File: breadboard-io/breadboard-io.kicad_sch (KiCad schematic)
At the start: 29 parts, among them J1 Conn_01x10_Male, Q1 DMN3300U, Q2 DMN3300U, Q3 DMN3300U, Q4 DMN3300U, SW1 SW0, SW2 SW0, SW3 SW0, SW4 SW0

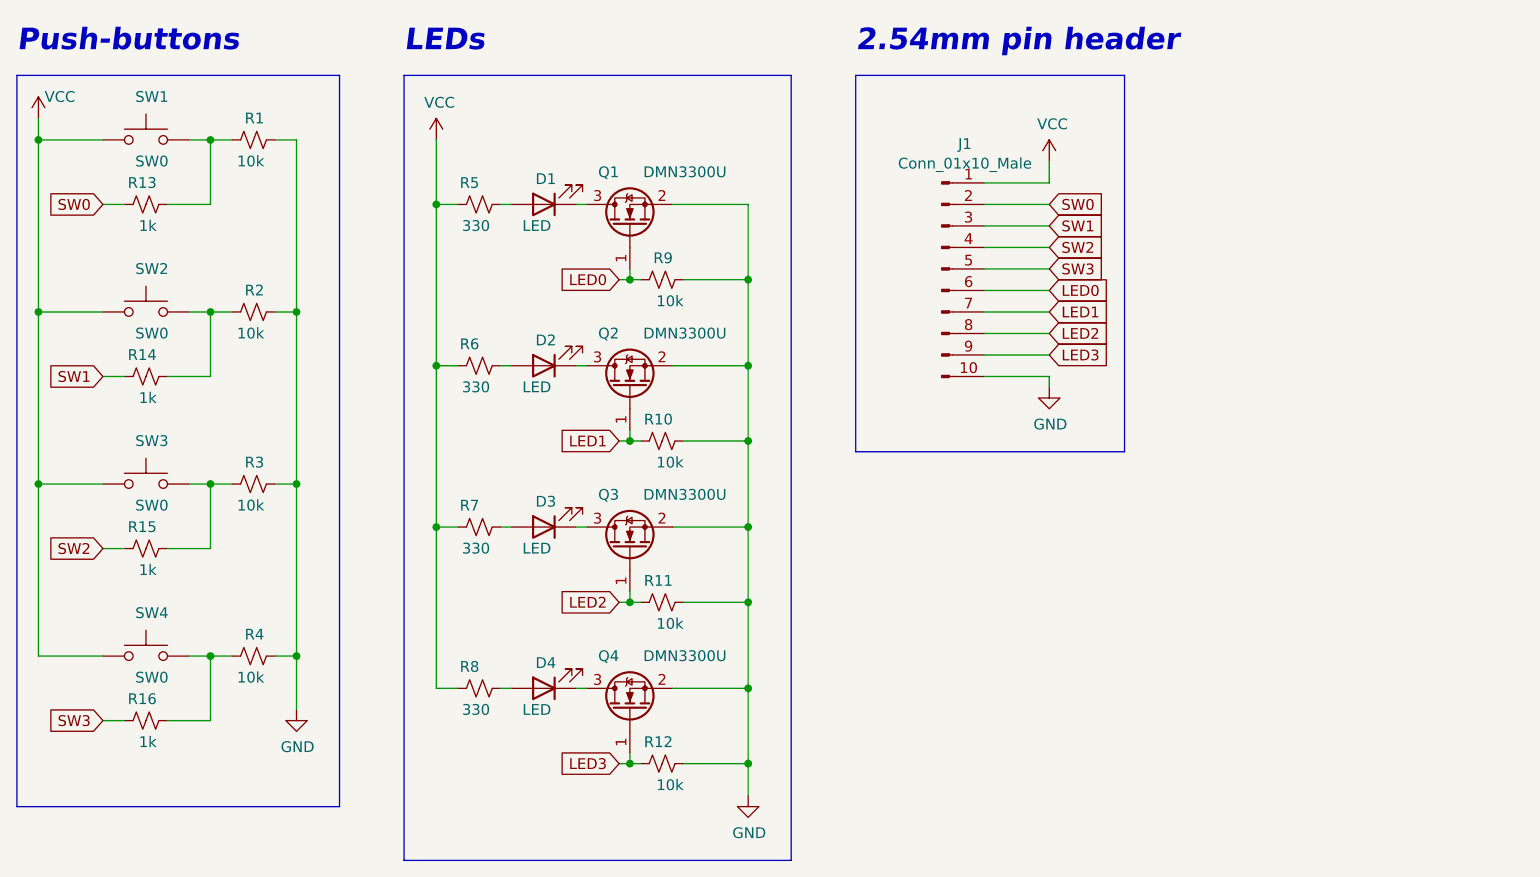
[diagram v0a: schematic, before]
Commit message: Testing schematic generation with hierachial sheets
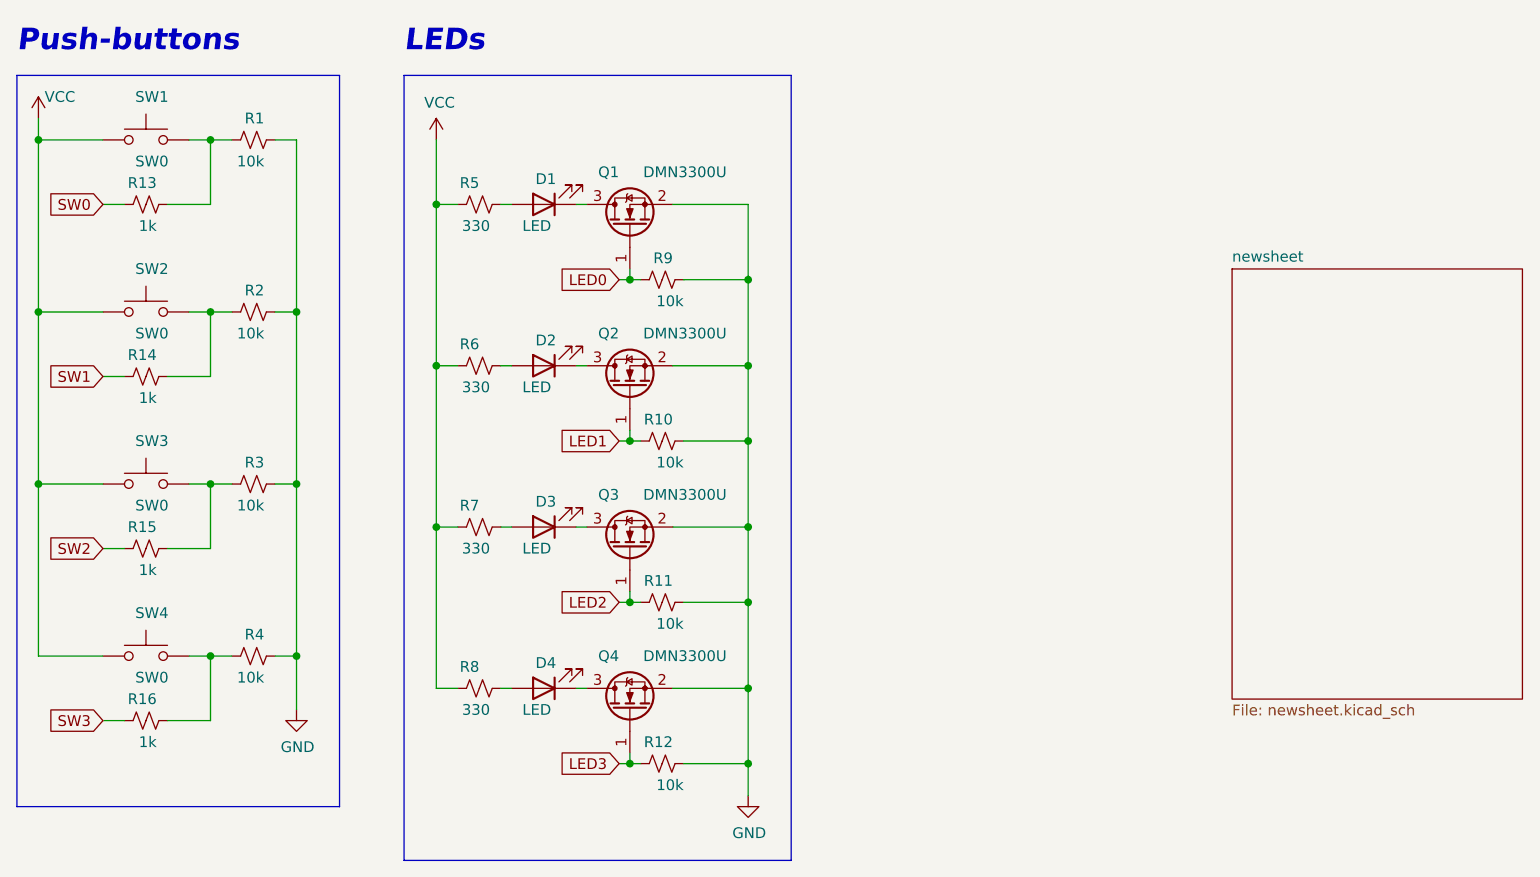
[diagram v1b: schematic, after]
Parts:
- removed J1: Conn_01x10_Male, Connector_PinHeader_2.54mm:PinHeader_1x10_P2.54mm_Horizontal, symbol Connector:Conn_01x10_Male
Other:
- added sheet newsheet (newsheet.kicad_sch)
- note removed: "2.54mm pin header"

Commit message: Moved schematic back to a single sheet
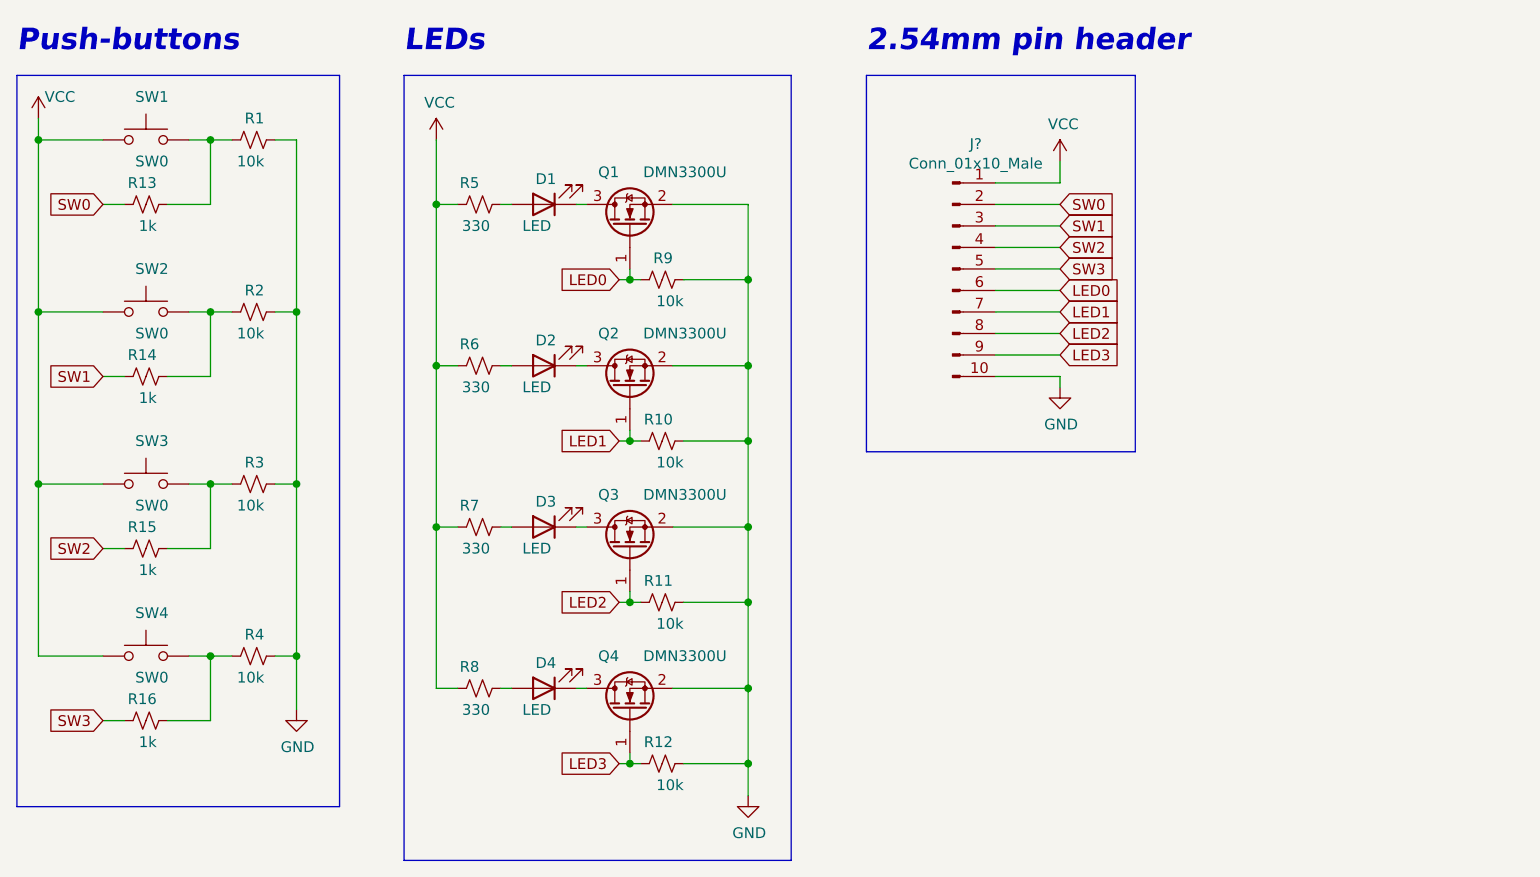
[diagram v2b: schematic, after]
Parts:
- added J?: Conn_01x10_Male, Connector_PinHeader_2.54mm:PinHeader_1x10_P2.54mm_Horizontal, symbol Connector:Conn_01x10_Male
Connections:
- net GND: now also J?.10 (Pin_10)
- net LED0: now also J?.6 (Pin_6)
- net LED1: now also J?.7 (Pin_7)
- net LED2: now also J?.8 (Pin_8)
- net LED3: now also J?.9 (Pin_9)
- net SW0: now also J?.2 (Pin_2)
- net SW1: now also J?.3 (Pin_3)
- net SW2: now also J?.4 (Pin_4)
- net SW3: now also J?.5 (Pin_5)
- net VCC: now also J?.1 (Pin_1)
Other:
- removed sheet newsheet
- note added: "2.54mm pin header"

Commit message: Updated schematic w/ MFP parts
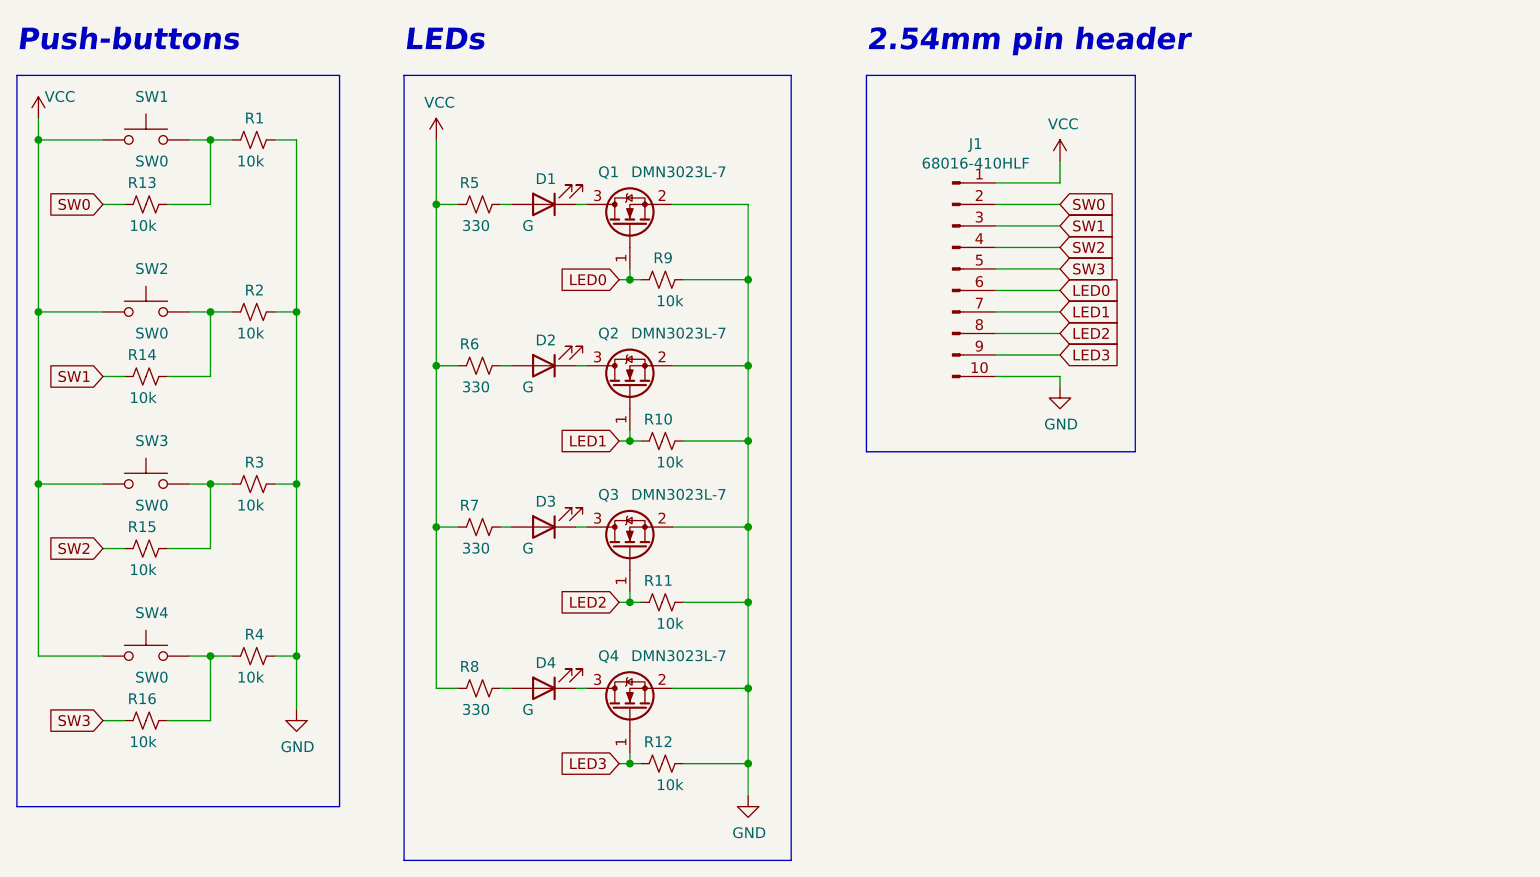
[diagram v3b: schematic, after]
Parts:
- D1, D2, D3, D4: value LED -> G; MFP (none) -> 150060VS55040
- J1: renamed from J?; value Conn_01x10_Male -> 68016-410HLF; MFP (none) -> 68016-410HLF
- Q1, Q2, Q3, Q4: value DMN3300U -> DMN3023L-7; MFP (none) -> DMN3023L-7
- R1, R2, R3, R4: MFP (none) -> RC0402FR-0710KL
- R13, R14, R15, R16: value 1k -> 10k; MFP (none) -> RC0402FR-0710KL
- R5, R6, R7, R8: MFP (none) -> RC0402FR-07330RL
- SW1, SW2, SW3, SW4: MFP (none) -> EVQ-P7A01P

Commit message: Added everyday dev logo in silk
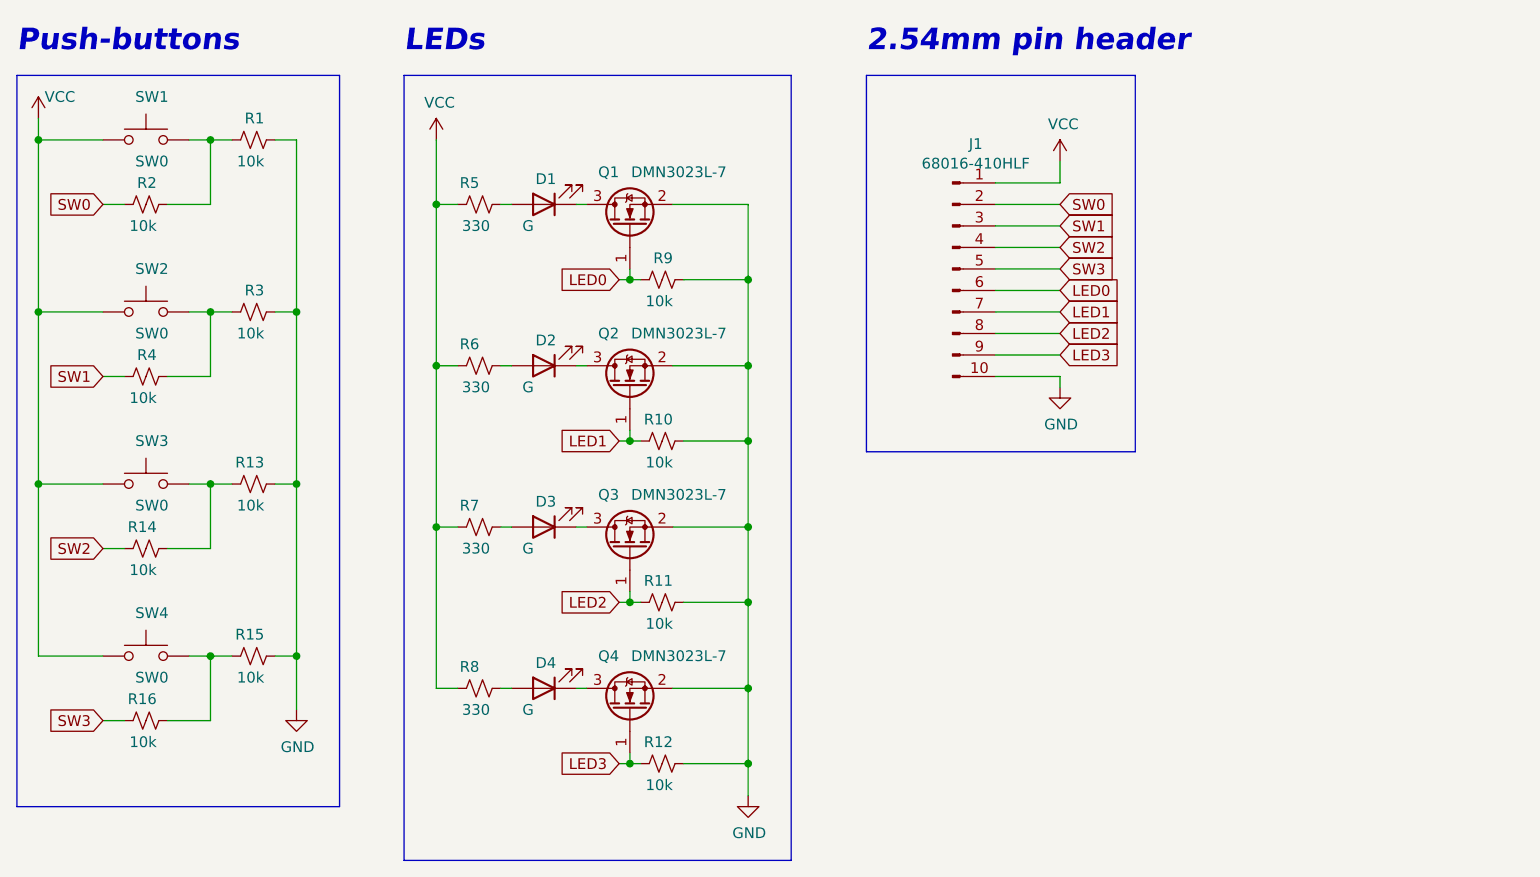
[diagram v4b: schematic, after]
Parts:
- D1, D2, D3, D4: MFP 150060VS55040 -> (none); MPN (none) -> 150060VS55040; Manufacturer (none) -> Würth Elektronik
- J1: MFP 68016-410HLF -> (none); MPN (none) -> 68016-410HLF; Manufacturer (none) -> Amphenol ICC (FCI)
- Q1, Q2, Q3, Q4: MFP DMN3023L-7 -> (none); MPN (none) -> DMN3023L-7; Manufacturer (none) -> Diodes Incorporated
- R1, R13, R14, R15, R16, R2, R3, R4: MFP RC0402FR-0710KL -> (none); MPN (none) -> RC0402FR-0710KL; Manufacturer (none) -> YAGEO
- R10, R11, R12, R9: MPN (none) -> RC0402FR-0710KL; Manufacturer (none) -> YAGEO
- R5, R6, R7, R8: MFP RC0402FR-07330RL -> (none); MPN (none) -> RC0402FR-07330RL; Manufacturer (none) -> YAGEO
- SW1, SW2, SW3, SW4: MFP EVQ-P7A01P -> (none); MPN (none) -> EVQ-P7A01P; Manufacturer (none) -> Panasonic
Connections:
- net GND: now also R13.2, R15.2; no longer R2.2, R4.2
- net SW0: now also R2.1; no longer R13.1
- net SW1: now also R4.1; no longer R14.1
- net SW2: now also R14.1; no longer R15.1
- net at R1.1, SW1.2: now also R2.2; no longer R13.2
- net at R16.2, SW4.2: now also R15.1; no longer R4.1
- new net: R3.1, R4.2, SW2.2
- new net: R13.1, R14.2, SW3.2
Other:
- company: great lakes dev -> everyday dev
